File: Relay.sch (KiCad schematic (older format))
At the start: 0 parts

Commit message: Module 3, Unit 5: Understanding The Relay Module
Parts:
- added D?: LED, symbol LED
- added D?: DIODE, symbol DIODE
- added K?: SPDT, symbol SPDT
- added Q?: NPN, symbol NPN
- added R? (x6): R, symbol R
- added U?: PHTRANS, symbol PHTRANS
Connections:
- net DIN+: now also U?.1
- net DIN-: now also R?.1
- new net: R?.2, U?.2
- new net: D?.1 (A), R?.1, U?.4
- new net: D?.2 (K), K?.2 (COIL+), R?.1, R?.2, U?.5
- new net: R?.1, U?.6
- new net: Q?.2 (B), R?.2
- new net: Q?.1 (E), R?.2
- new net: D?.1 (A), K?.5 (COIL-), Q?.3 (C)
- new net: D?.2 (K), R?.2
- new net +12V: R?.2
- new net COM: K?.1 (COM)
- new net GND: R?.1, R?.1
- new net NC: K?.4 (NC)
- new net NO: K?.3 (NO)
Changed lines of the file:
@@
 LIBS:contrib
 LIBS:valves
+LIBS:BenchBudEE
 LIBS:BenchBudEE-cache
 EELAYER 24 0
@@
 Comment4 ""
 $EndDescr
-Text HLabel 2000 2550 0    60   Input ~ 0
+Text HLabel 2500 3200 0    60   Input ~ 0
 DIN+
-Text HLabel 2000 2800 0    60   Output ~ 0
+Text HLabel 2500 3550 0    60   Output ~ 0
 DIN-
-Text HLabel 9800 2600 0    60   Input ~ 0
-Relay+
-Text HLabel 9800 2850 0    60   Output ~ 0
-Relay-
+Text HLabel 10500 2600 2    60   BiDi ~ 0
+NC
+Text HLabel 10500 2800 2    60   BiDi ~ 0
+NO
+$Comp
+L PHTRANS U?
+U 1 1 53012FD3
+P 4950 3400
+F 0 "U?" H 4900 3750 70  0000 C CNN
+F 1 "PHTRANS" H 4900 3050 70  0000 C CNN
+F 2 "" H 4950 3400 60  0000 C CNN
+F 3 "" H 4950 3400 60  0000 C CNN
+	1    4950 3400
+	1    0    0    -1
+$EndComp
+$Comp
+L R R?
+U 1 1 53012FF1
+P 6500 3600
+F 0 "R?" V 6580 3600 40  0000 C CNN
+F 1 "R" V 6507 3601 40  0000 C CNN
+F 2 "" V 6430 3600 30  0000 C CNN
+F 3 "" H 6500 3600 30  0000 C CNN
+	1    6500 3600
+	0    -1   -1   0
+$EndComp
+$Comp
+L NPN Q?
+U 1 1 53013005
+P 9000 4050
+F 0 "Q?" H 9000 3900 50  0000 R CNN
+F 1 "NPN" H 9000 4200 50  0000 R CNN
+F 2 "" H 9000 4050 60  0000 C CNN
+F 3 "" H 9000 4050 60  0000 C CNN
+	1    9000 4050
+	1    0    0    -1
+$EndComp
+$Comp
+L LED D?
+U 1 1 53013023
+P 6000 4000
+F 0 "D?" H 6000 4100 50  0000 C CNN
+F 1 "LED" H 6000 3900 50  0000 C CNN
+F 2 "" H 6000 4000 60  0000 C CNN
+F 3 "" H 6000 4000 60  0000 C CNN
+	1    6000 4000
+	0    1    1    0
+$EndComp
+$Comp
+L SPDT K?
+U 1 1 5301353C
+P 9700 2650
+F 0 "K?" H 9700 2900 70  0000 C CNN
+F 1 "SPDT" H 9700 2100 70  0000 C CNN
+F 2 "" H 9700 2650 60  0000 C CNN
+F 3 "" H 9700 2650 60  0000 C CNN
+	1    9700 2650
+	1    0    0    -1
+$EndComp
+Text HLabel 10500 2200 2    60   BiDi ~ 0
+COM
+Wire Wire Line
+	10100 2600 10500 2600
+Wire Wire Line
+	10100 2800 10500 2800
+Wire Wire Line
+	5500 3600 6250 3600
+Wire Wire Line
+	9100 3000 9300 3000
+$Comp
+L GND #PWR?
+U 1 1 53013B82
+P 9100 5300
+F 0 "#PWR?" H 9100 5300 30  0001 C CNN
+F 1 "GND" H 9100 5230 30  0001 C CNN
+F 2 "" H 9100 5300 60  0000 C CNN
+F 3 "" H 9100 5300 60  0000 C CNN
+	1    9100 5300
+	1    0    0    -1
+$EndComp
+$Comp
+L R R?
+U 1 1 53013B9D
+P 9100 4700
+F 0 "R?" V 9180 4700 40  0000 C CNN
+F 1 "R" V 9107 4701 40  0000 C CNN
+F 2 "" V 9030 4700 30  0000 C CNN
+F 3 "" H 9100 4700 30  0000 C CNN
+	1    9100 4700
+	-1   0    0    1
+$EndComp
+Wire Wire Line
+	9100 4950 9100 5300
+$Comp
+L R R?
+U 1 1 53013BD9
+P 6000 4650
+F 0 "R?" V 6080 4650 40  0000 C CNN
+F 1 "R" V 6007 4651 40  0000 C CNN
+F 2 "" V 5930 4650 30  0000 C CNN
+F 3 "" H 6000 4650 30  0000 C CNN
+	1    6000 4650
+	-1   0    0    1
+$EndComp
+Wire Wire Line
+	6000 3800 6000 3600
+Connection ~ 6000 3600
+Wire Wire Line
+	6000 4200 6000 4400
+Wire Wire Line
+	6000 4900 6000 5100
+Wire Wire Line
+	6000 5100 9100 5100
+Connection ~ 9100 5100
+$Comp
+L R R?
+U 1 1 53013C23
+P 6400 2150
+F 0 "R?" V 6480 2150 40  0000 C CNN
+F 1 "R" V 6407 2151 40  0000 C CNN
+F 2 "" V 6330 2150 30  0000 C CNN
+F 3 "" H 6400 2150 30  0000 C CNN
+	1    6400 2150
+	-1   0    0    1
+$EndComp
+$Comp
+L +12V #PWR?
+U 1 1 53013C30
+P 6400 1500
+F 0 "#PWR?" H 6400 1450 20  0001 C CNN
+F 1 "+12V" H 6400 1600 30  0000 C CNN
+F 2 "" H 6400 1500 60  0000 C CNN
+F 3 "" H 6400 1500 60  0000 C CNN
+	1    6400 1500
+	1    0    0    -1
+$EndComp
+Wire Wire Line
+	6400 1500 6400 1900
+Wire Wire Line
+	6400 2400 6400 3400
+Wire Wire Line
+	6400 2900 9300 2900
+Wire Wire Line
+	6400 3400 5500 3400
+Connection ~ 6400 2900
+$Comp
+L R R?
+U 1 1 53013C87
+P 5950 3200
+F 0 "R?" V 6030 3200 40  0000 C CNN
+F 1 "R" V 5957 3201 40  0000 C CNN
+F 2 "" V 5880 3200 30  0000 C CNN
+F 3 "" H 5950 3200 30  0000 C CNN
+	1    5950 3200
+	0    -1   -1   0
+$EndComp
+Wire Wire Line
+	5500 3200 5700 3200
+Wire Wire Line
+	6200 3200 6400 3200
+Connection ~ 6400 3200
+$Comp
+L R R?
+U 1 1 53013CC0
+P 3650 3550
+F 0 "R?" V 3730 3550 40  0000 C CNN
+F 1 "R" V 3657 3551 40  0000 C CNN
+F 2 "" V 3580 3550 30  0000 C CNN
+F 3 "" H 3650 3550 30  0000 C CNN
+	1    3650 3550
+	0    -1   -1   0
+$EndComp
+Wire Wire Line
+	2500 3200 4400 3200
+Wire Wire Line
+	3900 3550 4400 3550
+Wire Wire Line
+	3400 3550 2500 3550
+Wire Wire Line
+	10500 2200 9100 2200
+Wire Wire Line
+	9100 2200 9100 2700
+Wire Wire Line
+	9100 2700 9300 2700
+$Comp
+L DIODE D?
+U 1 1 53013E0F
+P 8300 3250
+F 0 "D?" H 8300 3350 40  0000 C CNN
+F 1 "DIODE" H 8300 3150 40  0000 C CNN
+F 2 "" H 8300 3250 60  0000 C CNN
+F 3 "" H 8300 3250 60  0000 C CNN
+	1    8300 3250
+	0    -1   -1   0
+$EndComp
+Wire Wire Line
+	9100 3000 9100 3850
+Wire Wire Line
+	8300 2900 8300 3050
+Connection ~ 8300 2900
+Wire Wire Line
+	8300 3450 8300 3650
+Wire Wire Line
+	8300 3650 9100 3650
+Connection ~ 9100 3650
+Wire Wire Line
+	9100 4250 9100 4450
+Wire Wire Line
+	6750 3600 6900 3600
+Wire Wire Line
+	6900 3600 6900 4050
+Wire Wire Line
+	6900 4050 8800 4050
 $EndSCHEMATC

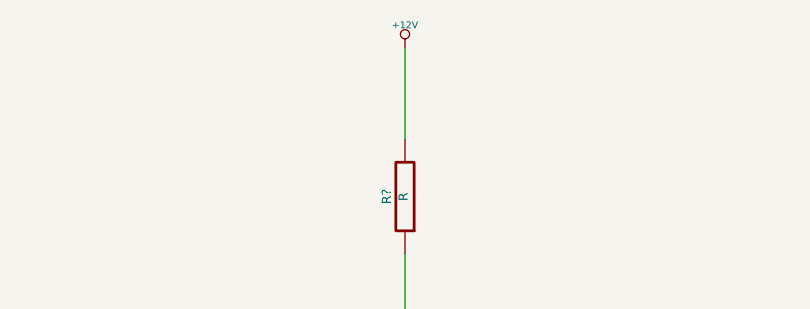
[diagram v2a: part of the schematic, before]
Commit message: Module 3, Unit 6: Understanding The Power Protection And Filtering Module
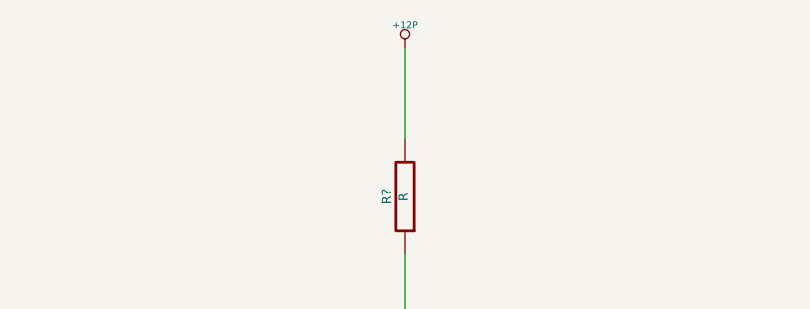
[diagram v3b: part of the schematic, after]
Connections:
- net +12V renamed +12P
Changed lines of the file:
@@
 $Descr A4 11693 8268
 encoding utf-8
-Sheet 4 8
+Sheet 4 9
 Title ""
 Date ""
@@
 	-1   0    0    1
 $EndComp
-$Comp
-L +12V #PWR?
-U 1 1 53013C30
-P 6400 1500
-F 0 "#PWR?" H 6400 1450 20  0001 C CNN
-F 1 "+12V" H 6400 1600 30  0000 C CNN
-F 2 "" H 6400 1500 60  0000 C CNN
-F 3 "" H 6400 1500 60  0000 C CNN
-	1    6400 1500
-	1    0    0    -1
-$EndComp
-Wire Wire Line
-	6400 1500 6400 1900
 Wire Wire Line
 	6400 2400 6400 3400
@@
 Wire Wire Line
 	6900 4050 8800 4050
+$Comp
+L +12P #PWR?
+U 1 1 530155CB
+P 6400 1500
+F 0 "#PWR?" H 6400 1470 30  0001 C CNN
+F 1 "+12P" H 6400 1600 30  0000 C CNN
+F 2 "" H 6400 1500 60  0000 C CNN
+F 3 "" H 6400 1500 60  0000 C CNN
+	1    6400 1500
+	1    0    0    -1
+$EndComp
+Wire Wire Line
+	6400 1500 6400 1900
 $EndSCHEMATC

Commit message: Module 3, Unit 9: Understanding The Arduino Module
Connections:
- net COM renamed RELAY_COM
- net DIN+ renamed RELAY+
- net DIN- renamed RELAY-
- net NC renamed RELAY_NC
- net NO renamed RELAY_NO
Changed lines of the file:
@@
 $EndDescr
 Text HLabel 2500 3200 0    60   Input ~ 0
-DIN+
+RELAY+
 Text HLabel 2500 3550 0    60   Output ~ 0
-DIN-
+RELAY-
 Text HLabel 10500 2600 2    60   BiDi ~ 0
-NC
+RELAY_NC
 Text HLabel 10500 2800 2    60   BiDi ~ 0
-NO
+RELAY_NO
 $Comp
 L PHTRANS U?
@@
 $EndComp
 Text HLabel 10500 2200 2    60   BiDi ~ 0
-COM
+RELAY_COM
 Wire Wire Line
 	10100 2600 10500 2600
